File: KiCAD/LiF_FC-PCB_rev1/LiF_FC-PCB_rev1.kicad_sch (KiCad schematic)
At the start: 0 parts

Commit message: added test sheets for merge test
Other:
- added sheet Test Sheet Main 2 (Test Sheet Main 2.kicad_sch)
- added sheet Test_sheet_main (Test_sheet_main.kicad_sch)
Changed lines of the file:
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@@
 	(generator_version "9.0")
 	(paper "A4")
+	(sheet
+		(at 86.36 64.77)
+		(size 29.21 30.48)
+		(exclude_from_sim no)
+		(in_bom yes)
+		(on_board yes)
+		(dnp no)
+		(fields_autoplaced yes)
+		(stroke
+			(width 0.1524)
+			(type solid)
+		)
+		(fill
+			(color 0 0 0 0.0000)
+		)
+		(property "Sheetname" "Test_sheet_main"
+			(at 86.36 64.0584 0)
+			(effects
+				(font
+					(size 1.27 1.27)
+				)
+				(justify left bottom)
+			)
+		)
+		(property "Sheetfile" "Test_sheet_main.kicad_sch"
+			(at 86.36 95.8346 0)
+			(effects
+				(font
+					(size 1.27 1.27)
+				)
+				(justify left top)
+			)
+		)
+		(property "Field2" ""
+			(at 86.36 64.77 0)
+			(effects
+				(font
+					(size 1.27 1.27)
+				)
+			)
+		)
+		(instances
+			(project "LiF_FC-PCB_rev1"
+				(path "/9e3e8da7-e506-46c9-90e5-307e4ad30d29"
+					(page "2")
+				)
+			)
+		)
+	)
+	(sheet
+		(at 157.48 66.04)
+		(size 35.56 35.56)
+		(exclude_from_sim no)
+		(in_bom yes)
+		(on_board yes)
+		(dnp no)
+		(fields_autoplaced yes)
+		(stroke
+			(width 0.1524)
+			(type solid)
+		)
+		(fill
+			(color 0 0 0 0.0000)
+		)
+		(property "Sheetname" "Test Sheet Main 2"
+			(at 157.48 65.3284 0)
+			(effects
+				(font
+					(size 1.27 1.27)
+				)
+				(justify left bottom)
+			)
+		)
+		(property "Sheetfile" "Test Sheet Main 2.kicad_sch"
+			(at 157.48 102.1846 0)
+			(effects
+				(font
+					(size 1.27 1.27)
+				)
+				(justify left top)
+			)
+		)
+		(instances
+			(project "LiF_FC-PCB_rev1"
+				(path "/9e3e8da7-e506-46c9-90e5-307e4ad30d29"
+					(page "3")
+				)
+			)
+		)
+	)
 	(sheet_instances
 		(path "/"

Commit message: added stuff on main sheet and merged main into here
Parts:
- added R3: R, symbol Device:R
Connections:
- new net Test Sheet Main 2/hello: R3.2
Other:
- sheet Test Sheet Main 2 ports: added hello; removed none
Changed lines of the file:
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@@
 	(generator_version "9.0")
 	(paper "A4")
+	(wire
+		(pts
+			(xy 135.89 91.44) (xy 135.89 114.3)
+		)
+		(stroke
+			(width 0)
+			(type default)
+		)
+	)
+	(wire
+		(pts
+			(xy 157.48 91.44) (xy 135.89 91.44)
+		)
+		(stroke
+			(width 0)
+			(type default)
+		)
+	)
+	(wire
+		(pts
+			(xy 135.89 114.3) (xy 148.59 114.3)
+		)
+		(stroke
+			(width 0)
+			(type default)
+		)
+	)
+	(wire
+		(pts
+			(xy 148.59 110.49) (xy 148.59 114.3)
+		)
+		(stroke
+			(width 0)
+			(type default)
+		)
+	)
+	(symbol
+		(lib_id "Device:R")
+		(at 148.59 106.68 0)
+		(unit 1)
+		(exclude_from_sim no)
+		(in_bom yes)
+		(on_board yes)
+		(dnp no)
+		(fields_autoplaced yes)
+		(property "Reference" "R3"
+			(at 151.13 105.4099 0)
+			(effects
+				(font
+					(size 1.27 1.27)
+				)
+				(justify left)
+			)
+		)
+		(property "Value" "R"
+			(at 151.13 107.9499 0)
+			(effects
+				(font
+					(size 1.27 1.27)
+				)
+				(justify left)
+			)
+		)
+		(property "Footprint" ""
+			(at 146.812 106.68 90)
+			(effects
+				(font
+					(size 1.27 1.27)
+				)
+				(hide yes)
+			)
+		)
+		(property "Datasheet" "~"
+			(at 148.59 106.68 0)
+			(effects
+				(font
+					(size 1.27 1.27)
+				)
+				(hide yes)
+			)
+		)
+		(property "Description" "Resistor"
+			(at 148.59 106.68 0)
+			(effects
+				(font
+					(size 1.27 1.27)
+				)
+				(hide yes)
+			)
+		)
+		(pin "1"
+		)
+		(pin "2"
+		)
+		(instances
+			(project ""
+				(path "/9e3e8da7-e506-46c9-90e5-307e4ad30d29"
+					(reference "R3")
+					(unit 1)
+				)
+			)
+		)
+	)
 	(sheet
 		(at 86.36 64.77)
@@
 			)
 		)
+		(pin "hello" input
+			(at 157.48 91.44 180)
+			(effects
+				(font
+					(size 1.27 1.27)
+				)
+				(justify left)
+			)
+		)

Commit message: setting up an actual KiCAD project, removing test sheets
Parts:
- removed R3: R, symbol Device:R
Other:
- removed sheet Test Sheet Main 2
- removed sheet Test_sheet_main
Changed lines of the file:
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@@
 	(generator_version "9.0")
 	(paper "A4")
-	(wire
-		(pts
-			(xy 135.89 91.44) (xy 135.89 114.3)
-		)
-		(stroke
-			(width 0)
-			(type default)
-		)
-	)
-	(wire
-		(pts
-			(xy 157.48 91.44) (xy 135.89 91.44)
-		)
-		(stroke
-			(width 0)
-			(type default)
-		)
-	)
-	(wire
-		(pts
-			(xy 135.89 114.3) (xy 148.59 114.3)
-		)
-		(stroke
-			(width 0)
-			(type default)
-		)
-	)
-	(wire
-		(pts
-			(xy 148.59 110.49) (xy 148.59 114.3)
-		)
-		(stroke
-			(width 0)
-			(type default)
-		)
-	)
-	(symbol
-		(lib_id "Device:R")
-		(at 148.59 106.68 0)
-		(unit 1)
-		(exclude_from_sim no)
-		(in_bom yes)
-		(on_board yes)
-		(dnp no)
-		(fields_autoplaced yes)
-		(property "Reference" "R3"
-			(at 151.13 105.4099 0)
-			(effects
-				(font
-					(size 1.27 1.27)
-				)
-				(justify left)
-			)
-		)
-		(property "Value" "R"
-			(at 151.13 107.9499 0)
-			(effects
-				(font
-					(size 1.27 1.27)
-				)
-				(justify left)
-			)
-		)
-		(property "Footprint" ""
-			(at 146.812 106.68 90)
-			(effects
-				(font
-					(size 1.27 1.27)
-				)
-				(hide yes)
-			)
-		)
-		(property "Datasheet" "~"
-			(at 148.59 106.68 0)
-			(effects
-				(font
-					(size 1.27 1.27)
-				)
-				(hide yes)
-			)
-		)
-		(property "Description" "Resistor"
-			(at 148.59 106.68 0)
-			(effects
-				(font
-					(size 1.27 1.27)
-				)
-				(hide yes)
-			)
-		)
-		(pin "1"
-		)
-		(pin "2"
-		)
-		(instances
-			(project ""
-				(path "/9e3e8da7-e506-46c9-90e5-307e4ad30d29"
-					(reference "R3")
-					(unit 1)
-				)
-			)
-		)
-	)
-	(sheet
-		(at 86.36 64.77)
-		(size 29.21 30.48)
-		(exclude_from_sim no)
-		(in_bom yes)
-		(on_board yes)
-		(dnp no)
-		(fields_autoplaced yes)
-		(stroke
-			(width 0.1524)
-			(type solid)
-		)
-		(fill
-			(color 0 0 0 0.0000)
-		)
-		(property "Sheetname" "Test_sheet_main"
-			(at 86.36 64.0584 0)
-			(effects
-				(font
-					(size 1.27 1.27)
-				)
-				(justify left bottom)
-			)
-		)
-		(property "Sheetfile" "Test_sheet_main.kicad_sch"
-			(at 86.36 95.8346 0)
-			(effects
-				(font
-					(size 1.27 1.27)
-				)
-				(justify left top)
-			)
-		)
-		(property "Field2" ""
-			(at 86.36 64.77 0)
-			(effects
-				(font
-					(size 1.27 1.27)
-				)
-			)
-		)
-		(instances
-			(project "LiF_FC-PCB_rev1"
-				(path "/9e3e8da7-e506-46c9-90e5-307e4ad30d29"
-					(page "2")
-				)
-			)
-		)
-	)
-	(sheet
-		(at 157.48 66.04)
-		(size 35.56 35.56)
-		(exclude_from_sim no)
-		(in_bom yes)
-		(on_board yes)
-		(dnp no)
-		(fields_autoplaced yes)
-		(stroke
-			(width 0.1524)
-			(type solid)
-		)
-		(fill
-			(color 0 0 0 0.0000)
-		)
-		(property "Sheetname" "Test Sheet Main 2"
-			(at 157.48 65.3284 0)
-			(effects
-				(font
-					(size 1.27 1.27)
-				)
-				(justify left bottom)
-			)
-		)
-		(property "Sheetfile" "Test Sheet Main 2.kicad_sch"
-			(at 157.48 102.1846 0)
-			(effects
-				(font
-					(size 1.27 1.27)
-				)
-				(justify left top)
-			)
-		)
-		(pin "hello" input
-			(at 157.48 91.44 180)
-			(effects
-				(font
-					(size 1.27 1.27)
-				)
-				(justify left)
-			)
-		)
-		(instances
-			(project "LiF_FC-PCB_rev1"
-				(path "/9e3e8da7-e506-46c9-90e5-307e4ad30d29"
-					(page "3")
-				)
-			)
-		)
-	)
 	(sheet_instances
 		(path "/"

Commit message: added power or-ing and power regulation circuits
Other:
- added sheet Power Regulation (LiF_PowerReg.kicad_sch)
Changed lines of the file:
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@@
 	(generator_version "9.0")
 	(paper "A4")
+	(sheet
+		(at 193.04 100.33)
+		(size 36.83 17.78)
+		(exclude_from_sim no)
+		(in_bom yes)
+		(on_board yes)
+		(dnp no)
+		(fields_autoplaced yes)
+		(stroke
+			(width 0.1524)
+			(type solid)
+		)
+		(fill
+			(color 0 0 0 0.0000)
+		)
+		(property "Sheetname" "Power Regulation"
+			(at 193.04 99.6184 0)
+			(effects
+				(font
+					(size 1.27 1.27)
+				)
+				(justify left bottom)
+			)
+		)
+		(property "Sheetfile" "LiF_PowerReg.kicad_sch"
+			(at 193.04 118.6946 0)
+			(effects
+				(font
+					(size 1.27 1.27)
+				)
+				(justify left top)
+			)
+		)
+		(pin "A3V3" output
+			(at 229.87 115.57 0)
+			(effects
+				(font
+					(size 1.27 1.27)
+				)
+				(justify right)
+			)
+		)
+		(pin "A3V3_{EN}" input
+			(at 193.04 115.57 180)
+			(effects
+				(font
+					(size 1.27 1.27)
+				)
+				(justify left)
+			)
+		)
+		(pin "R3V3" output
+			(at 229.87 109.22 0)
+			(effects
+				(font
+					(size 1.27 1.27)
+				)
+				(justify right)
+			)
+		)
+		(pin "R3V3_{EN}" input
+			(at 193.04 113.03 180)
+			(effects
+				(font
+					(size 1.27 1.27)
+				)
+				(justify left)
+			)
+		)
+		(pin "R5V0" output
+			(at 229.87 102.87 0)
+			(effects
+				(font
+					(size 1.27 1.27)
+				)
+				(justify right)
+			)
+		)
+		(pin "V_{IN1}" input
+			(at 193.04 102.87 180)
+			(effects
+				(font
+					(size 1.27 1.27)
+				)
+				(justify left)
+			)
+		)
+		(pin "V_{IN2}" input
+			(at 193.04 107.95 180)
+			(effects
+				(font
+					(size 1.27 1.27)
+				)
+				(justify left)
+			)
+		)
+		(instances
+			(project "LiF_FC-PCB_rev1"
+				(path "/9e3e8da7-e506-46c9-90e5-307e4ad30d29"
+					(page "3")
+				)
+			)
+		)
+	)
 	(sheet_instances
 		(path "/"

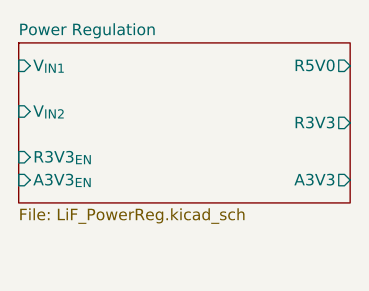
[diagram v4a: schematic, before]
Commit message: changed 5V regulator to support 5V in up to 20V in
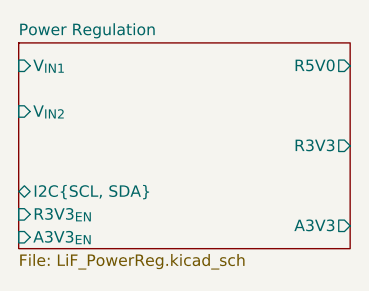
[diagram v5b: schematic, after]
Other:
- sheet Power Regulation ports: added I2C{SCL, SDA}; removed none
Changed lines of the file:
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@@
 	(sheet
 		(at 193.04 100.33)
-		(size 36.83 17.78)
+		(size 36.83 22.86)
 		(exclude_from_sim no)
 		(in_bom yes)
@@
 		)
 		(property "Sheetfile" "LiF_PowerReg.kicad_sch"
-			(at 193.04 118.6946 0)
+			(at 193.04 123.7746 0)
 			(effects
 				(font
@@
 		)
 		(pin "A3V3" output
-			(at 229.87 115.57 0)
+			(at 229.87 120.65 0)
 			(effects
 				(font
@@
 		)
 		(pin "A3V3_{EN}" input
-			(at 193.04 115.57 180)
+			(at 193.04 121.92 180)
 			(effects
 				(font
@@
 		)
 		(pin "R3V3" output
-			(at 229.87 109.22 0)
+			(at 229.87 111.76 0)
 			(effects
 				(font
@@
 		)
 		(pin "R3V3_{EN}" input
-			(at 193.04 113.03 180)
+			(at 193.04 119.38 180)
 			(effects
 				(font
@@
 			(effects
 				(font
+					(size 1.27 1.27)
+				)
+				(justify left)
+			)
+		)
+		(pin "I2C{SCL, SDA}" bidirectional
+			(at 193.04 116.84 180)
+			(effects
+				(font
